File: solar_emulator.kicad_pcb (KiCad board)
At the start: 2 copper layers, 125.5 x 77 mm, 69 parts, among them J1 USB_C_Receptacle_USB2.0_16P, J2 Conn_01x02, J3 Conn_01x02, J4 Conn_01x02, J5 Conn_01x02, J6 Conn_01x03, J7 Conn_01x04, Q1 IRFZ44N, Q2 IRFZ44N, Q3 IRFZ44N, Q4 IRFZ44N, Q5 IRFZ44N, Q6 IRFZ44N, Q7 IRFZ44N, Q8 IRFZ44N, SW1 SW_Push, SW2 SW_Push, U1 ESP32-S3-WROOM-1, U2 LD1117S33TR_SOT223, U3 HIP4081AIPZ, U4 HIP4081AIPZ, U5 LM393, U6 LM393

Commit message: PCB component layout complete, possible refinement needed
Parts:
- added C12: 10u, Capacitor_SMD:C_0603_1608Metric_Pad1.08x0.95mm_HandSolder, F.Cu at (158.8, 117.7)
- added F1: Fuse_Small, Fuse:Fuse_1206_3216Metric_Pad1.42x1.75mm_HandSolder, F.Cu at (155.6, 122.0)
- added U7: USBLC6-2SC6, Package_TO_SOT_SMD:SOT-23-6, F.Cu at (162.1, 118.0)
- C1, C4: footprint Capacitor_THT:C_Disc_D9.0mm_W2.5mm_P5.00mm -> Capacitor_SMD:C_0603_1608Metric_Pad1.08x0.95mm_HandSolder
- C10, C11, C5, C6, C7, C8, C9: footprint Capacitor_THT:C_Disc_D4.7mm_W2.5mm_P5.00mm -> Capacitor_SMD:C_0603_1608Metric_Pad1.08x0.95mm_HandSolder
- C2, C3: footprint Capacitor_THT:C_Disc_D6.0mm_W2.5mm_P5.00mm -> Capacitor_SMD:C_0603_1608Metric_Pad1.08x0.95mm_HandSolder
- D4, D5, D6, D7: footprint Diode_THT:D_DO-41_SOD81_P10.16mm_Horizontal -> Diode_SMD:D_SOD-123
- J2, J3, J4, J5: footprint Connector_PinHeader_2.54mm:PinHeader_1x02_P2.54mm_Vertical -> Connector_JST:JST_PH_B2B-PH-K_1x02_P2.00mm_Vertical
- J6: footprint Connector_PinHeader_2.54mm:PinHeader_1x03_P2.54mm_Vertical -> Connector_JST:JST_PH_B3B-PH-K_1x03_P2.00mm_Vertical
- J7: footprint Connector_PinHeader_2.54mm:PinHeader_1x04_P2.54mm_Vertical -> Connector_JST:JST_PH_B4B-PH-K_1x04_P2.00mm_Vertical
- R10, R11, R12, R13, R14, R15, R16, R17, R18, R19, R20, R21, R22, R23, R24, R27, R28, R29, R30, R4, R5, R6, R7, R8, R9: footprint Resistor_THT:R_Axial_DIN0207_L6.3mm_D2.5mm_P10.16mm_Horizontal -> Resistor_SMD:R_0805_2012Metric_Pad1.20x1.40mm_HandSolder
- R25, R26: footprint Resistor_THT:R_Axial_DIN0207_L6.3mm_D2.5mm_P15.24mm_Horizontal -> Resistor_SMD:R_0805_2012Metric_Pad1.20x1.40mm_HandSolder
- moved H1 137.5 mm to (231.8, 65.1), turned to 0 degrees
- moved H3 124.5 mm to (233.4, 131.8), turned to 0 degrees
- moved H2 120.2 mm to (146.8, 65.1), turned to 0 degrees
- moved H4 103.5 mm to (146.8, 131.8), turned to 0 degrees
- moved R16 65.2 mm to (172.8, 118.8), turned to 0 degrees
- moved R23 64.4 mm to (173.8, 84.3), turned to 0 degrees
- moved C6 63.9 mm to (225.1, 85.6), turned to -90 degrees
- moved R24 58.1 mm to (181.2, 114.0)
- moved R14 56.1 mm to (182.1, 79.5)
- moved D4 55.4 mm to (221.9, 85.7), turned to 90 degrees
- moved D7 53.3 mm to (223.4, 115.9)
- moved U5 53.3 mm to (177.6, 80.0), turned to 180 degrees
- moved U6 52.7 mm to (177.3, 118.3)
- moved C10 51.6 mm to (181.1, 71.5), turned to 90 degrees
- moved C11 50.8 mm to (173.9, 126.8), turned to -90 degrees
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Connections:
- J1 pad A4: +5V -> VBUS
- J1 pad A9: +5V -> VBUS
- J1 pad B4: +5V -> VBUS
- J1 pad B9: +5V -> VBUS
- U1 pad 13: D- -> USB_D-
- U1 pad 14: D+ -> USB_D+
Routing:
- net BHS2: track 76.6 -> 0.00 mm
- net BHS1: track 75.7 -> 0.00 mm
- net MOTOR3: track 58.9 -> 0.00 mm, vias 1 -> 0
- net BLS2: track 55.0 -> 0.00 mm, vias 1 -> 0
- net BHI1: track 53.1 -> 0.00 mm, vias 1 -> 0
- net MOTOR1: track 53.1 -> 0.00 mm
- net BLS1: track 53.0 -> 0.00 mm, vias 1 -> 0
- net AHI2: track 48.9 -> 0.00 mm, vias 1 -> 0
- net BLI1: track 48.4 -> 0.00 mm, vias 1 -> 0
- net ALI2: track 48.4 -> 0.00 mm, vias 1 -> 0
- net BLI2: track 47.9 -> 0.00 mm, vias 1 -> 0
- net AHI1: track 46.3 -> 0.00 mm, vias 1 -> 0
- net BHI2: track 45.3 -> 0.00 mm, vias 1 -> 0
- net ALI1: track 45.0 -> 0.00 mm, vias 1 -> 0
- net +3V3: track 38.0 -> 0.00 mm
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- removed copper zone on F.Cu, net +12V
- removed copper zone on F.Cu, net +3V3
- removed copper zone on B.Cu, net GND
- removed copper zone on F.Cu, net GND
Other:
- board outline removed

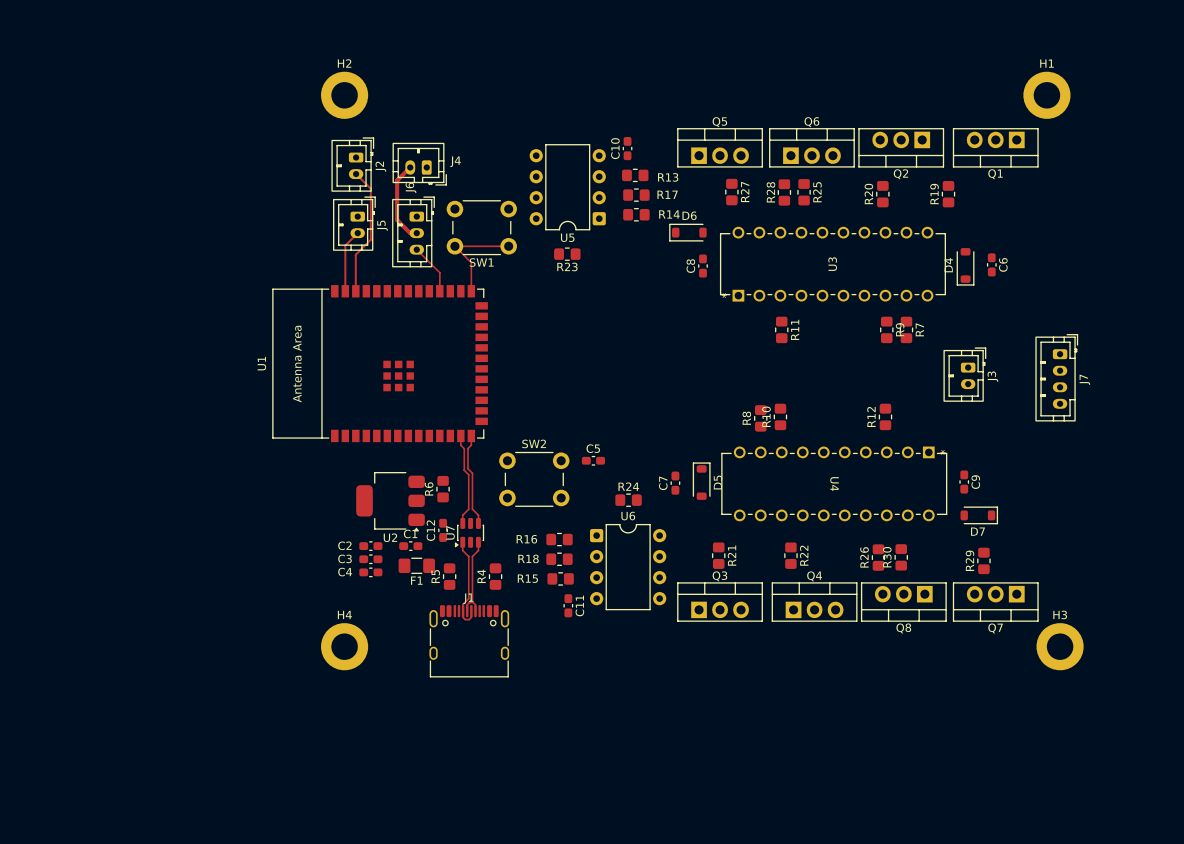
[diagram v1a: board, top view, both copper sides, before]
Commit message: add edge cuts to the pcb
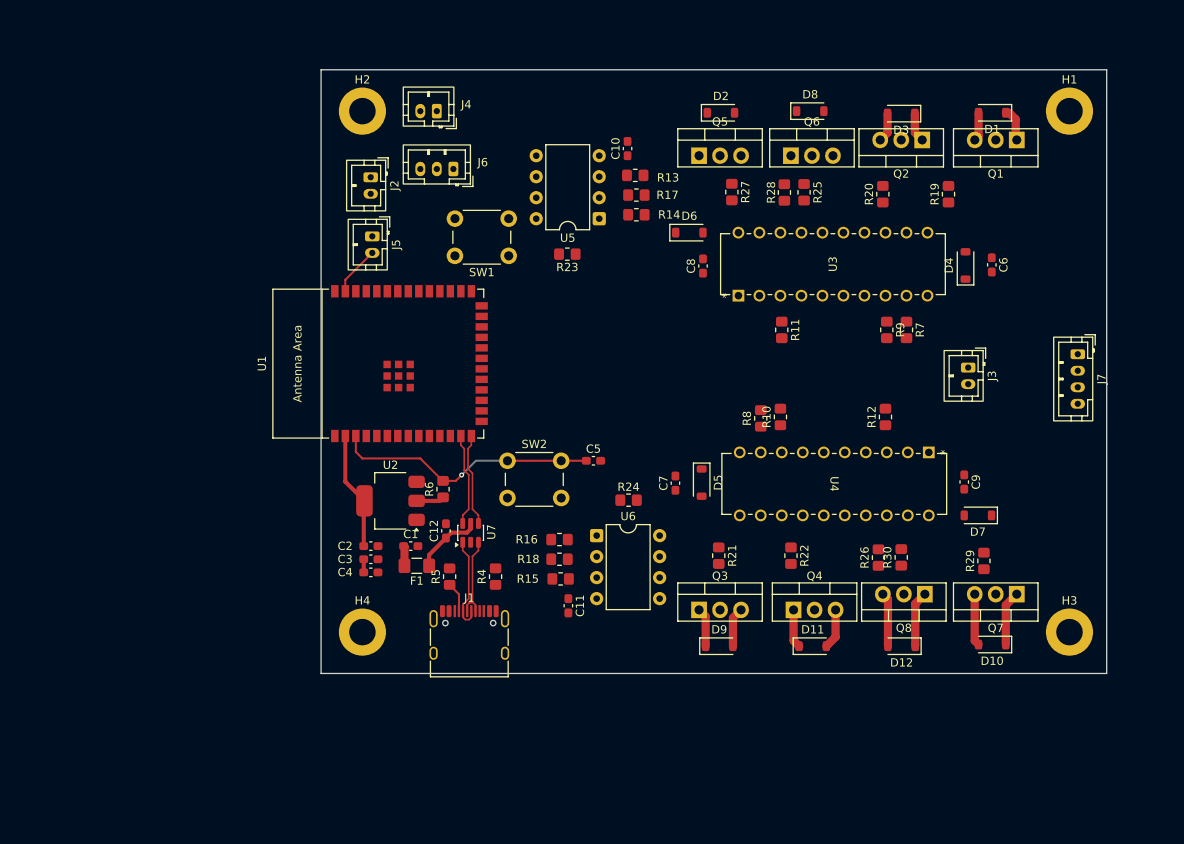
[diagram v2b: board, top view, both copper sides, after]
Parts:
- added D1: D_Zener, Diode_SMD:D_SOD-123, F.Cu at (225.2, 67.2)
- added D10: D_Zener, Diode_SMD:D_SOD-123, F.Cu at (225.2, 131.5)
- added D11: D_Zener, Diode_SMD:D_SOD-123, F.Cu at (203.4, 131.7)
- added D12: D_Zener, Diode_SMD:D_SOD-123, F.Cu at (214.2, 131.7)
- added D2: D_Zener, Diode_SMD:D_SOD-123, F.Cu at (192.3, 67.2)
- added D3: D_Zener, Diode_SMD:D_SOD-123, F.Cu at (214.2, 67.3)
- added D8: D_Zener, Diode_SMD:D_SOD-123, F.Cu at (203.2, 67.0)
- added D9: D_Zener, Diode_SMD:D_SOD-123, F.Cu at (192.2, 131.7)
- moved J6 7.26 mm to (160.0, 74.0), turned to 180 degrees
- moved J4 6.93 mm to (158.0, 67.0)
- moved H1 3.33 mm to (234.5, 67.0)
- moved J2 2.97 mm to (150.0, 75.0)
- moved J5 2.97 mm to (150.2, 82.1)
- moved H2 2.88 mm to (149.0, 67.0)
- moved H4 2.78 mm to (149.0, 130.0)
- moved J7 2.14 mm to (235.5, 96.4)
- moved H3 2.10 mm to (234.5, 130.0)
- moved SW1 1.16 mm to (166.7, 84.5)
- moved C12 0.36 mm to (159.1, 117.8)
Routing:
- net EN: track 0.00 -> 32.3 mm, vias 0 -> 1
- net +3V3: track 0.00 -> 19.3 mm
- net LIMIT1: track 15.7 -> 0.00 mm
- net +12V: track 0.00 -> 15.4 mm
- net BHS2: track 0.00 -> 13.0 mm
- net GPIO0: track 12.8 -> 0.00 mm
- net BLS2: track 0.00 -> 11.4 mm
- net 5V: track 10.0 -> 0.00 mm
- net MOTOR3: track 0.00 -> 9.46 mm
- net VBUS: track 0.00 -> 8.30 mm
- net MOTOR1: track 0.00 -> 7.03 mm
- net SERVO: track 6.18 -> 0.00 mm
- net Net-(J1-CC1): track 0.00 -> 3.64 mm
- net BLS1: track 0.00 -> 3.55 mm
- net +5V: track 0.00 -> 2.42 mm
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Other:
- board outline added: 95 x 73 mm

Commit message: tracing complete, need to optimize pcb
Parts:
- moved R24 18.8 mm to (173.0, 131.0), turned to 0 degrees
- moved R16 11.3 mm to (181.3, 126.2), turned to 180 degrees
- moved C11 11.2 mm to (180.3, 117.6), turned to 90 degrees
- moved R18 8.90 mm to (181.3, 123.8), turned to 180 degrees
- moved R15 8.50 mm to (181.2, 121.4), turned to 180 degrees
- moved U6 8.37 mm to (176.8, 126.7), turned to 180 degrees
- moved J2 7.49 mm to (154.0, 81.3)
- moved J5 2.28 mm to (148.1, 81.3)
- moved R25 1.59 mm to (204.0, 76.8), turned to 0 degrees
- moved R26 1.20 mm to (210.2, 121.0), turned to 180 degrees
- moved R28 0.79 mm to (200.8, 76.8)
- moved J4 0.75 mm to (158.8, 67.0)
- moved J6 0.75 mm to (160.8, 74.0)
- moved J1 0.26 mm to (161.9, 131.8)
- moved R10 0.18 mm to (199.5, 104.2)
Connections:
- U1 pad 15: AHI2 -> unconnected-(U1-GPIO3/TOUCH3/ADC1_CH2-Pad15)
- U1 pad 16: ALI2 -> unconnected-(U1-GPIO46-Pad16)
- U1 pad 17: BLI2 -> AHI2
- U1 pad 18: BHI2 -> ALI2
- U1 pad 19: unconnected-(U1-GPIO11/TOUCH11/ADC2_CH0/FSPID/FSPIIO5/SUBSPID-Pad19) -> BLI2
- U1 pad 20: unconnected-(U1-GPIO12/TOUCH12/ADC2_CH1/FSPICLK/FSPIIO6/SUBSPICLK-Pad20) -> BHI2
- U1 pad 21: unconnected-(U1-GPIO13/TOUCH13/ADC2_CH2/FSPIQ/FSPIIO7/SUBSPIQ-Pad21) -> AHI1
- U1 pad 22: unconnected-(U1-GPIO14/TOUCH14/ADC2_CH3/FSPIWP/FSPIDQS/SUBSPIWP-Pad22) -> ALI1
- U1 pad 23: AHI1 -> BLI1
- U1 pad 24: ALI1 -> BHI1
- U1 pad 25: BLI1 -> unconnected-(U1-GPIO48/SPICLK_N/SUBSPICLK_N_DIFF-Pad25)
- U1 pad 26: BHI1 -> unconnected-(U1-GPIO45-Pad26)
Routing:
- net +12V: track 15.4 -> 161.5 mm, vias 0 -> 1
- net +3V3: track 19.3 -> 119.3 mm, vias 0 -> 1
- net BHS1: track 0.15 -> 81.0 mm
- net MOTOR3: track 9.46 -> 73.0 mm, vias 0 -> 1
- net BHI2: track 0.00 -> 60.2 mm
- net AHI1: track 0.00 -> 51.3 mm
- net ALI1: track 0.00 -> 49.4 mm
- net BLI2: track 0.00 -> 49.1 mm
- net BHS2: track 13.0 -> 61.0 mm, vias 0 -> 1
- net BLI1: track 0.00 -> 48.0 mm
- net MOTOR1: track 7.03 -> 54.2 mm, vias 0 -> 1
- net BLS1: track 3.55 -> 50.7 mm, vias 0 -> 1
- net ALI2: track 0.00 -> 47.0 mm
- net AHI2: track 0.00 -> 45.3 mm
- net BLS2: track 11.4 -> 50.6 mm, vias 0 -> 1
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- added copper zone on B.Cu, net GND
- added copper zone on F.Cu, net GND

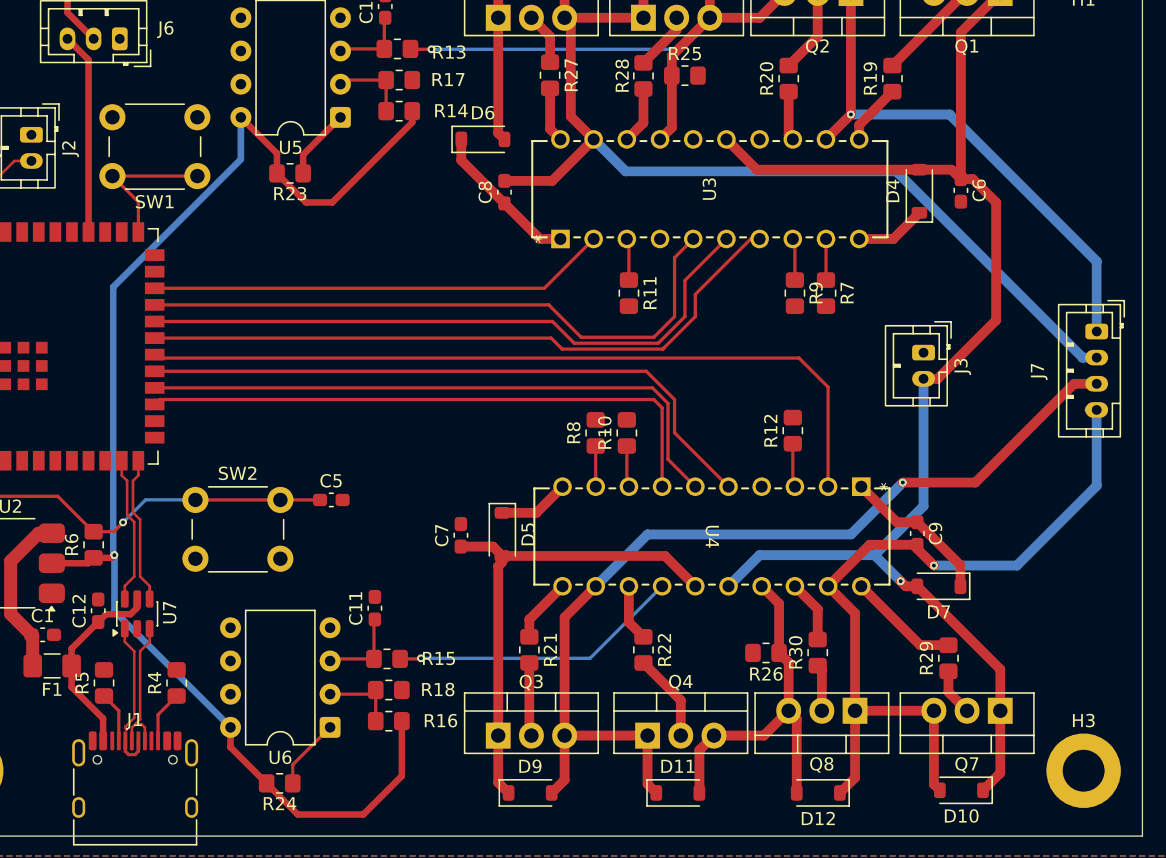
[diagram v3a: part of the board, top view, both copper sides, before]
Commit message: resolve some DRC errors, still need to check DRC
change copper fill from 1 oz to 2 oz, pad clearance 0.5 to 0.25mm

add some missing traces

focus on resolving DRC issues, and seek feedback
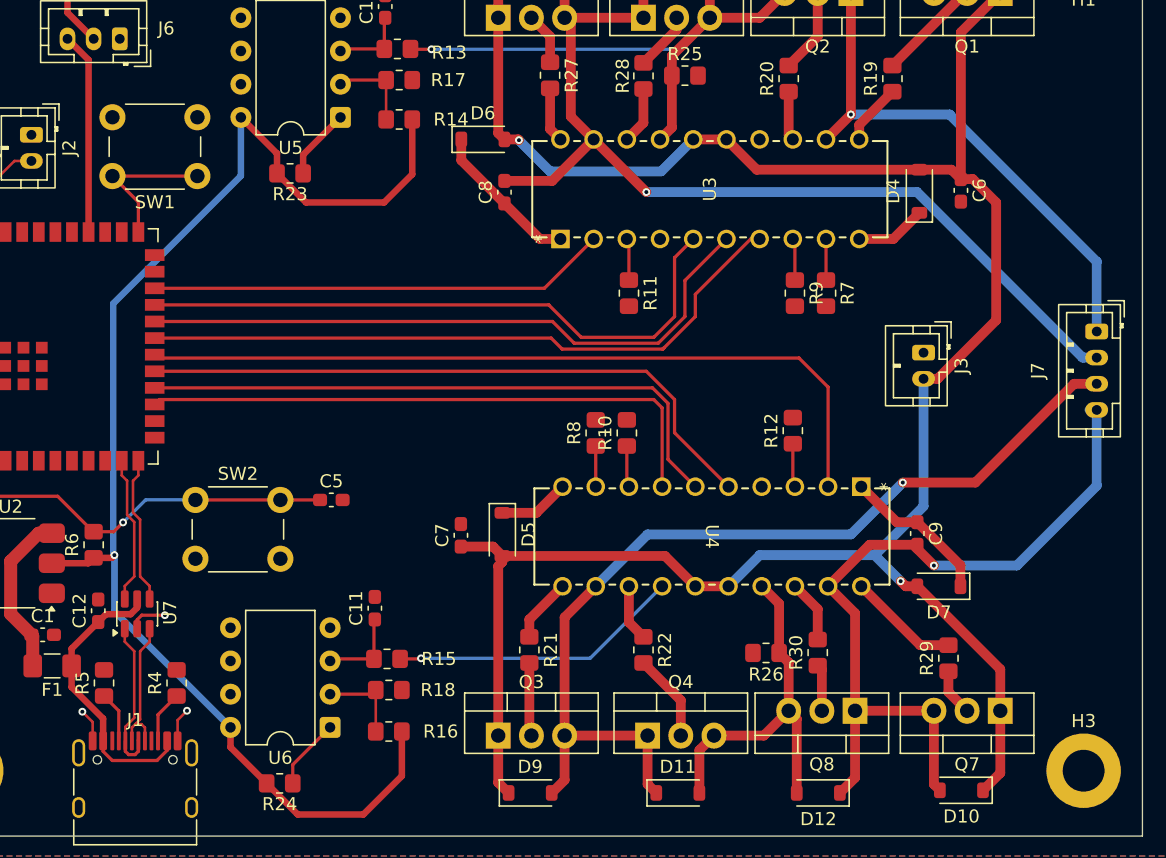
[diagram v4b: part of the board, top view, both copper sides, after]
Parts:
- moved R16 0.79 mm to (181.3, 127.0)
- moved R14 0.64 mm to (182.1, 80.2)
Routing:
- net +12V: track 161.5 -> 183.1 mm, vias 1 -> 2
- net GND: track 0.00 -> 8.12 mm, vias 0 -> 3
- net VBUS: track 16.2 -> 23.3 mm
- net +3V3: track 119.3 -> 120.2 mm
- net Net-(U6A--): track 6.01 -> 6.80 mm
- net D-: track 11.5 -> 12.3 mm
- net Net-(U5A--): track 6.01 -> 6.64 mm
- net BHS1: vias 0 -> 1

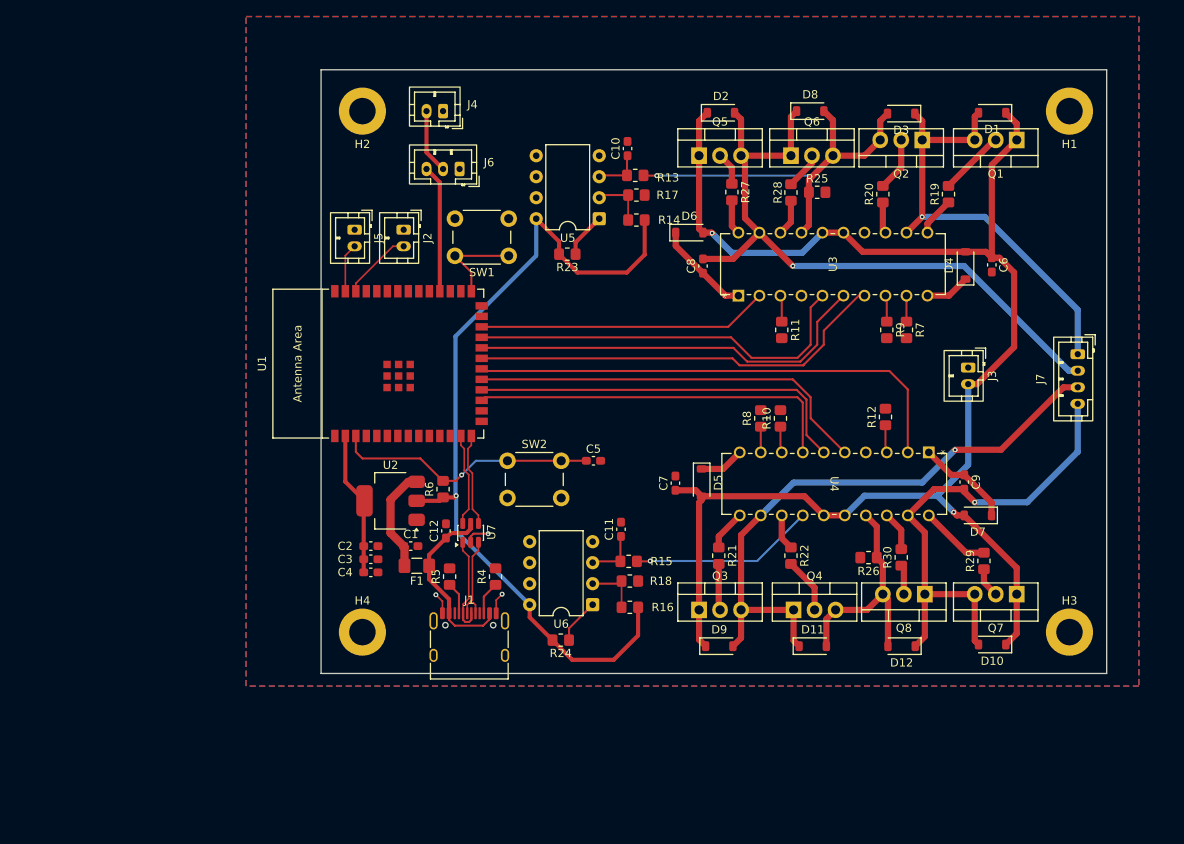
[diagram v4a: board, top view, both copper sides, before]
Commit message: add silk screen text, adjust buttons
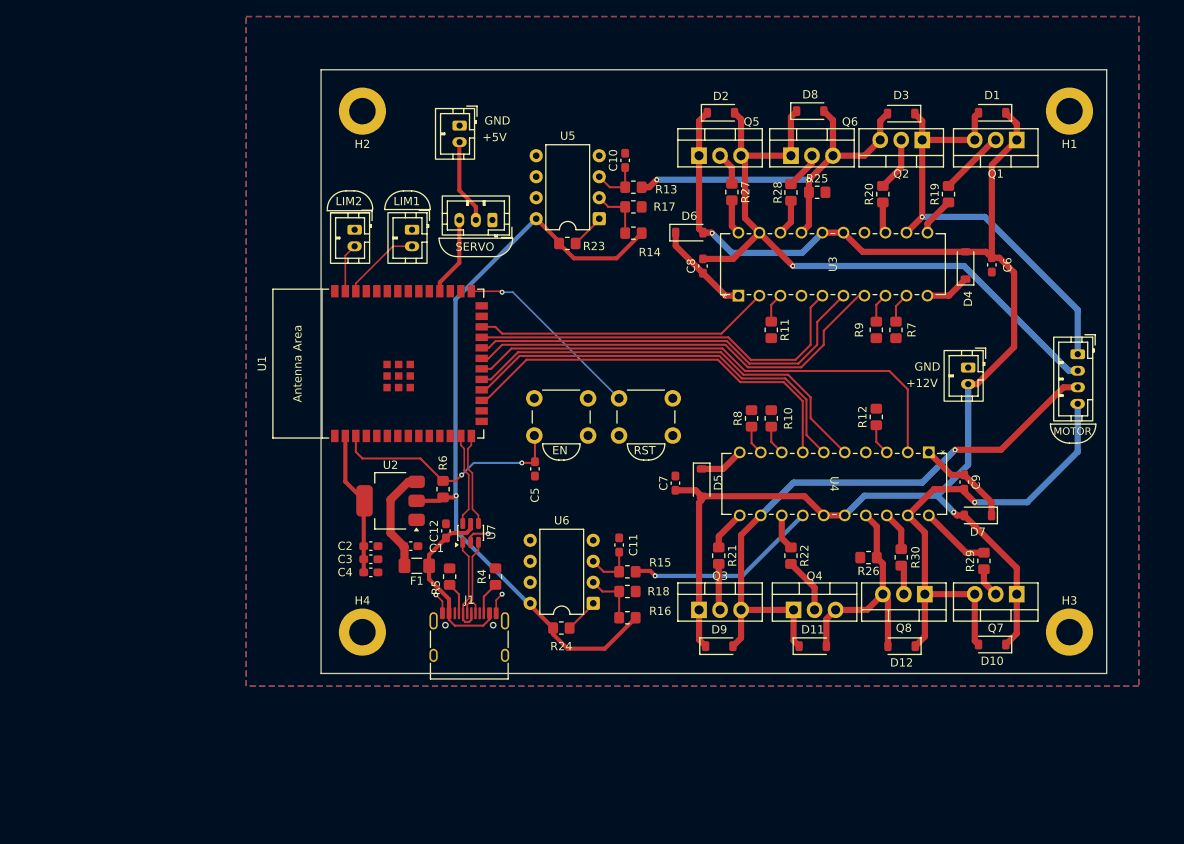
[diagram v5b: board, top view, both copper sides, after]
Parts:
- moved SW1 21.8 mm to (180.0, 101.7), turned to 0 degrees
- moved SW2 10.2 mm to (176.3, 106.2), turned to 180 degrees
- moved J6 7.34 mm to (164.7, 80.2)
- moved C5 7.14 mm to (169.9, 110.3), turned to -90 degrees
- moved J4 2.66 mm to (160.8, 68.8), turned to -90 degrees
- moved C11 1.91 mm to (180.0, 119.5)
- moved R14 1.63 mm to (181.8, 81.8)
- moved R17 1.47 mm to (181.8, 78.6)
- moved R24 1.46 mm to (173.1, 129.5)
- moved C10 1.46 mm to (180.8, 73.0)
- moved R13 1.45 mm to (181.8, 76.2)
- moved R16 1.30 mm to (181.0, 128.3)
- moved R18 1.30 mm to (181.0, 125.1)
- moved R23 1.30 mm to (173.8, 83.0)
- moved R15 1.27 mm to (181.0, 122.7)
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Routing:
- net GPIO0: track 11.6 -> 23.2 mm, vias 0 -> 1
- net +3V3: track 120.2 -> 110.2 mm
- net SERVO: track 15.4 -> 9.59 mm
- net AHI2: track 45.3 -> 49.1 mm
- net ALI2: track 47.0 -> 50.4 mm
- net BLS1: track 50.7 -> 47.4 mm, vias 1 -> 2
- net EN: track 32.3 -> 29.2 mm, vias 1 -> 2
- net BLI2: track 49.1 -> 51.8 mm
- net 5V: track 7.83 -> 10.4 mm
- net BHI2: track 60.2 -> 62.6 mm
- net AHI1: track 51.3 -> 52.7 mm
- net OCP2: track 5.47 -> 4.17 mm
- net OCP1: track 5.47 -> 4.31 mm
- net LIMIT1: track 8.60 -> 9.61 mm
- net BLS2: track 50.6 -> 51.6 mm
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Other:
- board text added: "+12V"
- board text added: "+5V"
- board text added: "EN"
- board text added: "GND"
- board text added: "LIM1"
- board text added: "LIM2"
- board text added: "MOTOR"
- board text added: "RST"
- board text added: "SERVO"

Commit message: implement small optimizations, GND vias
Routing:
- net GND: track 8.95 -> 23.7 mm, vias 3 -> 31
- net AHI2: track 49.1 -> 48.1 mm
- net BHI1: track 35.8 -> 35.2 mm
- net ALI2: track 50.4 -> 49.8 mm
